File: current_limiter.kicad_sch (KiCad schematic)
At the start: 53 parts, among them J1 73096-2, J2 73096-2, J3 CS-, J4 CS+, J5 73096-2, J6 73096-2, Q1 BSC040N10NS5, Q2 BC849, Q3 BC858, U1 TLV1805QDBVRQ1, U2 INA181A2IDBVR, U3 OPA991IDCKR, U4 BAT54CLT3G, U5 LM4040DIM3-2.5/NOPB

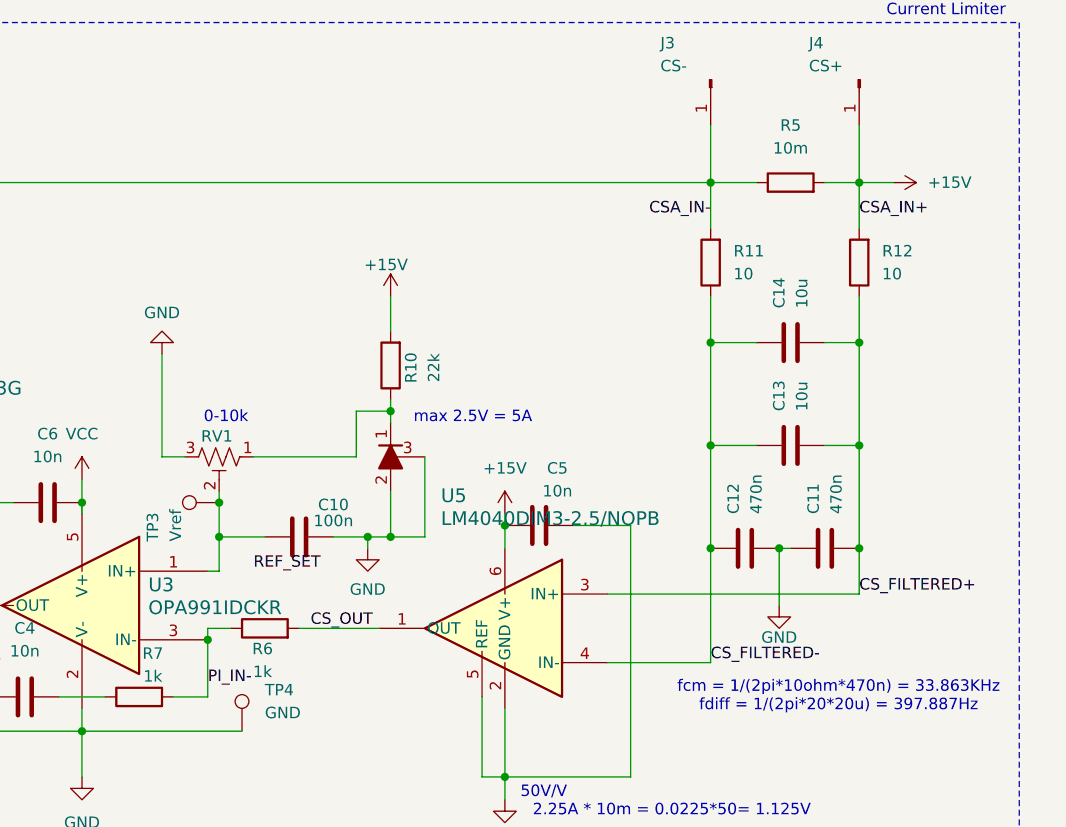
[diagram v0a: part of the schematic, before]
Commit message: minor updates: swapped out currentsense for in stock version, made sure all parts in stock, corrected Vs for currentsense
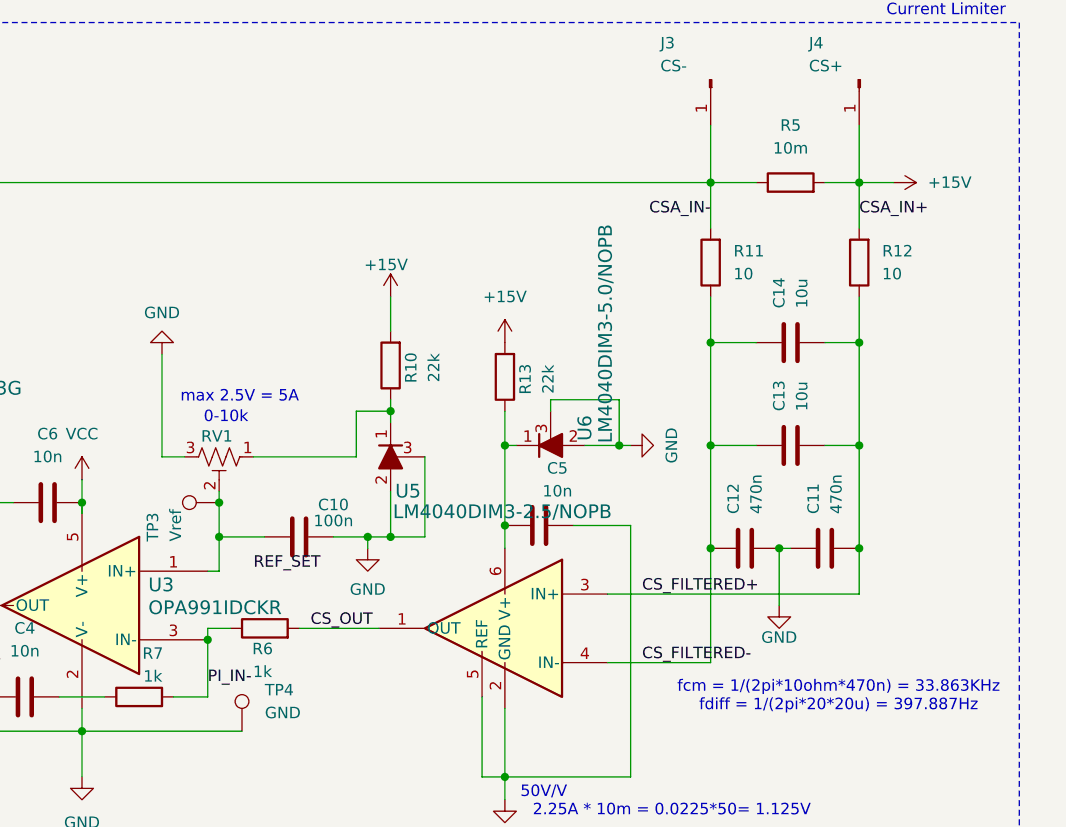
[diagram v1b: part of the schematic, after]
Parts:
- added R13: 22k, Capacitor_SMD:C_0805_2012Metric, symbol Device:R
- added U6: LM4040DIM3-5.0/NOPB, Current_Limiter_Stuff:DBZ3, symbol Current-limiter-stuff:LM4040DIM3-2.5_NOPB
- Q1: value BSC040N10NS5 -> ISC025N08NM5LF2
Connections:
- net +15V: now also R13.2; no longer C5.1, U2.6 (V+)
- net GND: now also U6.2, U6.3
- new net: C5.1, R13.1, U2.6 (V+), U6.1

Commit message: updated zeners to model thats actually in stock
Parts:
- removed D3, D5: BZV55B20, Diode_SMD:D_MiniMELF, symbol Diode:BZV55B20
- added CR1, CR2: BZT52C20-7-F, Current_Limiter_Stuff:SOD123_DIO, symbol Current-limiter-stuff:BZT52C20-7-F
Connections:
- net VBATT: now also CR1.1
- net fet_gate: now also CR2.1
- new net: CR1.2, CR2.2
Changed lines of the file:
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@@
 	)
 	(junction
+		(at 132.08 35.56)
+		(diameter 0)
+		(color 0 0 0 0)
+	)
+	(junction
 		(at 177.8 96.52)
 		(diameter 0)
@@
 	(wire
 		(pts
+			(xy 132.08 50.8) (xy 132.08 46.99)
+		)
+		(stroke
+			(width 0)
+			(type default)
+		)
+	)
+	(wire
+		(pts
 			(xy 186.69 66.04) (xy 189.23 66.04)
 		)
@@
 	(wire
 		(pts
+			(xy 121.92 40.64) (xy 121.92 46.99)
+		)
+		(stroke
+			(width 0)
+			(type default)
+		)
+	)
+	(wire
+		(pts
 			(xy 153.67 50.8) (xy 156.21 50.8)
 		)
@@
 	(wire
 		(pts
+			(xy 139.7 50.8) (xy 132.08 50.8)
+		)
+		(stroke
+			(width 0)
+			(type default)
+		)
+	)
+	(wire
+		(pts
 			(xy 99.06 46.99) (xy 99.06 54.61)
 		)
@@
 	(wire
 		(pts
-			(xy 128.27 50.8) (xy 139.7 50.8)
-		)
-		(stroke
-			(width 0)
-			(type default)
-		)
-	)
-	(wire
-		(pts
 			(xy 62.23 31.75) (xy 99.06 31.75)
 		)
@@
 	(wire
 		(pts
+			(xy 132.08 35.56) (xy 132.08 40.64)
+		)
+		(stroke
+			(width 0)
+			(type default)
+		)
+	)
+	(wire
+		(pts
 			(xy 193.04 69.85) (xy 193.04 71.12)
 		)
@@
 	)
 	(symbol
-		(lib_id "Diode:BZV55B20")
-		(at 128.27 39.37 270)
-		(unit 1)
-		(body_style 1)
-		(exclude_from_sim no)
-		(in_bom yes)
-		(on_board yes)
-		(in_pos_files yes)
-		(dnp no)
-		(fields_autoplaced yes)
-		(property "Reference" "D5"
-			(at 130.81 38.0999 90)
-			(show_name no)
-			(do_not_autoplace no)
-			(effects
-				(font
-					(size 1.27 1.27)
-				)
-				(justify left)
-			)
-		)
-		(property "Value" "BZV55B20"
-			(at 130.81 40.6399 90)
-			(show_name no)
-			(do_not_autoplace no)
-			(effects
-				(font
-					(size 1.27 1.27)
-				)
-				(justify left)
-			)
-		)
-		(property "Footprint" "Diode_SMD:D_MiniMELF"
-			(at 123.825 39.37 0)
-			(hide yes)
-			(show_name no)
-			(do_not_autoplace no)
-			(effects
-				(font
-					(size 1.27 1.27)
-				)
-			)
-		)
-		(property "Datasheet" "https://assets.nexperia.com/documents/data-sheet/BZV55_SER.pdf"
-			(at 128.27 39.37 0)
-			(hide yes)
-			(show_name no)
-			(do_not_autoplace no)
-			(effects
-				(font
-					(size 1.27 1.27)
-				)
-			)
-		)
-		(property "Description" "20V, 500mW, 2%, Zener diode, MiniMELF"
-			(at 128.27 39.37 0)
-			(hide yes)
-			(show_name no)
-			(do_not_autoplace no)
-			(effects
-				(font
-					(size 1.27 1.27)
-				)
-			)
-		)
-		(pin "1"
-		)
-		(pin "2"
-		)
-		(instances
-			(project "current_limiter"
-				(path "/9cad53dd-e6ec-4945-b0cd-3a61fa1e6914"
-					(reference "D5")
-					(unit 1)
-				)
-			)
-		)
-	)
-	(symbol
 		(lib_id "Device:R")
 		(at 139.7 62.23 180)
@@
 	)
 	(symbol
+		(lib_id "Current-limiter-stuff:BZT52C20-7-F")
+		(at 121.92 40.64 0)
+		(unit 1)
+		(body_style 1)
+		(exclude_from_sim no)
+		(in_bom yes)
+		(on_board yes)
+		(in_pos_files yes)
+		(dnp no)
+		(property "Reference" "CR1"
+			(at 116.84 36.576 0)
+			(show_name no)
+			(do_not_autoplace no)
+			(effects
+				(font
+					(size 1.524 1.524)
+				)
+			)
+		)
+		(property "Value" "BZT52C20-7-F"
+			(at 116.84 39.116 0)
+			(show_name no)
+			(do_not_autoplace no)
+			(effects
+				(font
+					(size 1.524 1.524)
+				)
+			)
+		)
+		(property "Footprint" "Current_Limiter_Stuff:SOD123_DIO"
+			(at 121.92 40.64 0)
+			(hide yes)
+			(show_name no)
+			(do_not_autoplace no)
+			(effects
+				(font
+					(size 1.27 1.27)
+					(italic yes)
+				)
+			)
+		)
+		(property "Datasheet" "BZT52C20-7-F"
+			(at 121.92 40.64 0)
+			(hide yes)
+			(show_name no)
+			(do_not_autoplace no)
+			(effects
+				(font
+					(size 1.27 1.27)
+					(italic yes)
+				)
+			)
+		)
+		(property "Description" ""
+			(at 121.92 40.64 0)
+			(hide yes)
+			(show_name no)
+			(do_not_autoplace no)
+			(effects
+				(font
+					(size 1.27 1.27)
+				)
+			)
+		)
+		(pin "1"
+		)
+		(pin "2"
+		)
+		(instances
+			(project "current_limiter"
+				(path "/9cad53dd-e6ec-4945-b0cd-3a61fa1e6914"
+					(reference "CR1")
+					(unit 1)
+				)
+			)
+		)
+	)
+	(symbol
 		(lib_id "Connector:TestPoint")
 		(at 195.58 96.52 0)
@@
 	)
 	(symbol
+		(lib_id "Current-limiter-stuff:BZT52C20-7-F")
+		(at 121.92 46.99 0)
+		(unit 1)
+		(body_style 1)
+		(exclude_from_sim no)
+		(in_bom yes)
+		(on_board yes)
+		(in_pos_files yes)
+		(dnp no)
+		(property "Reference" "CR2"
+			(at 137.922 52.07 0)
+			(show_name no)
+			(do_not_autoplace no)
+			(effects
+				(font
+					(size 1.524 1.524)
+				)
+			)
+		)
+		(property "Value" "BZT52C20-7-F"
+			(at 137.922 49.53 0)
+			(show_name no)
+			(do_not_autoplace no)
+			(effects
+				(font
+					(size 1.524 1.524)
+				)
+			)
+		)
+		(property "Footprint" "Current_Limiter_Stuff:SOD123_DIO"
+			(at 121.92 46.99 0)
+			(hide yes)
+			(show_name no)
+			(do_not_autoplace no)
+			(effects
+				(font
+					(size 1.27 1.27)
+					(italic yes)
+				)
+			)
+		)
+		(property "Datasheet" "BZT52C20-7-F"
+			(at 121.92 46.99 0)
+			(hide yes)
+			(show_name no)
+			(do_not_autoplace no)
+			(effects
+				(font
+					(size 1.27 1.27)
+					(italic yes)
+				)
+			)
+		)
+		(property "Description" ""
+			(at 121.92 46.99 0)
+			(hide yes)
+			(show_name no)
+			(do_not_autoplace no)
+			(effects
+				(font
+					(size 1.27 1.27)
+				)
+			)
+		)
+		(pin "1"
+		)
+		(pin "2"
+		)
+		(instances
+			(project "current_limiter"
+				(path "/9cad53dd-e6ec-4945-b0cd-3a61fa1e6914"
+					(reference "CR2")
+					(unit 1)
+				)
+			)
+		)
+	)
+	(symbol
 		(lib_id "Device:R")
 		(at 247.65 44.45 180)
@@
 					(unit 1)
 				)
-			)
-		)
-	)
-	(symbol
-		(lib_id "Diode:BZV55B20")
-		(at 128.27 46.99 90)
-		(unit 1)
-		(body_style 1)
-		(exclude_from_sim no)
-		(in_bom yes)
-		(on_board yes)
-		(in_pos_files yes)
-		(dnp no)
-		(fields_autoplaced yes)
-		(property "Reference" "D3"
-			(at 130.81 45.7199 90)
-			(show_name no)
-			(do_not_autoplace no)
-			(effects
-				(font
-					(size 1.27 1.27)
-				)
-				(justify right)
-			)
-		)
-		(property "Value" "BZV55B20"
-			(at 130.81 48.2599 90)
-			(show_name no)
-			(do_not_autoplace no)
-			(effects
-				(font
-					(size 1.27 1.27)
-				)
-				(justify right)
-			)
-		)
-		(property "Footprint" "Diode_SMD:D_MiniMELF"
-			(at 132.715 46.99 0)
-			(hide yes)
-			(show_name no)
-			(do_not_autoplace no)
-			(effects
-				(font
-					(size 1.27 1.27)
-				)
-			)
-		)
-		(property "Datasheet" "https://assets.nexperia.com/documents/data-sheet/BZV55_SER.pdf"
-			(at 128.27 46.99 0)
-			(hide yes)
-			(show_name no)
-			(do_not_autoplace no)
-			(effects
-				(font
-					(size 1.27 1.27)
-				)
-			)
-		)
-		(property "Description" "20V, 500mW, 2%, Zener diode, MiniMELF"
-			(at 128.27 46.99 0)
-			(hide yes)
-			(show_name no)
-			(do_not_autoplace no)
-			(effects
-				(font
-					(size 1.27 1.27)
-				)
-			)
-		)
-		(pin "1"
-		)
-		(pin "2"
-		)
-		(instances
-			(project "current_limiter"
-				(path "/9cad53dd-e6ec-4945-b0cd-3a61fa1e6914"
-					(reference "D3")
-					(unit 1)
-				)

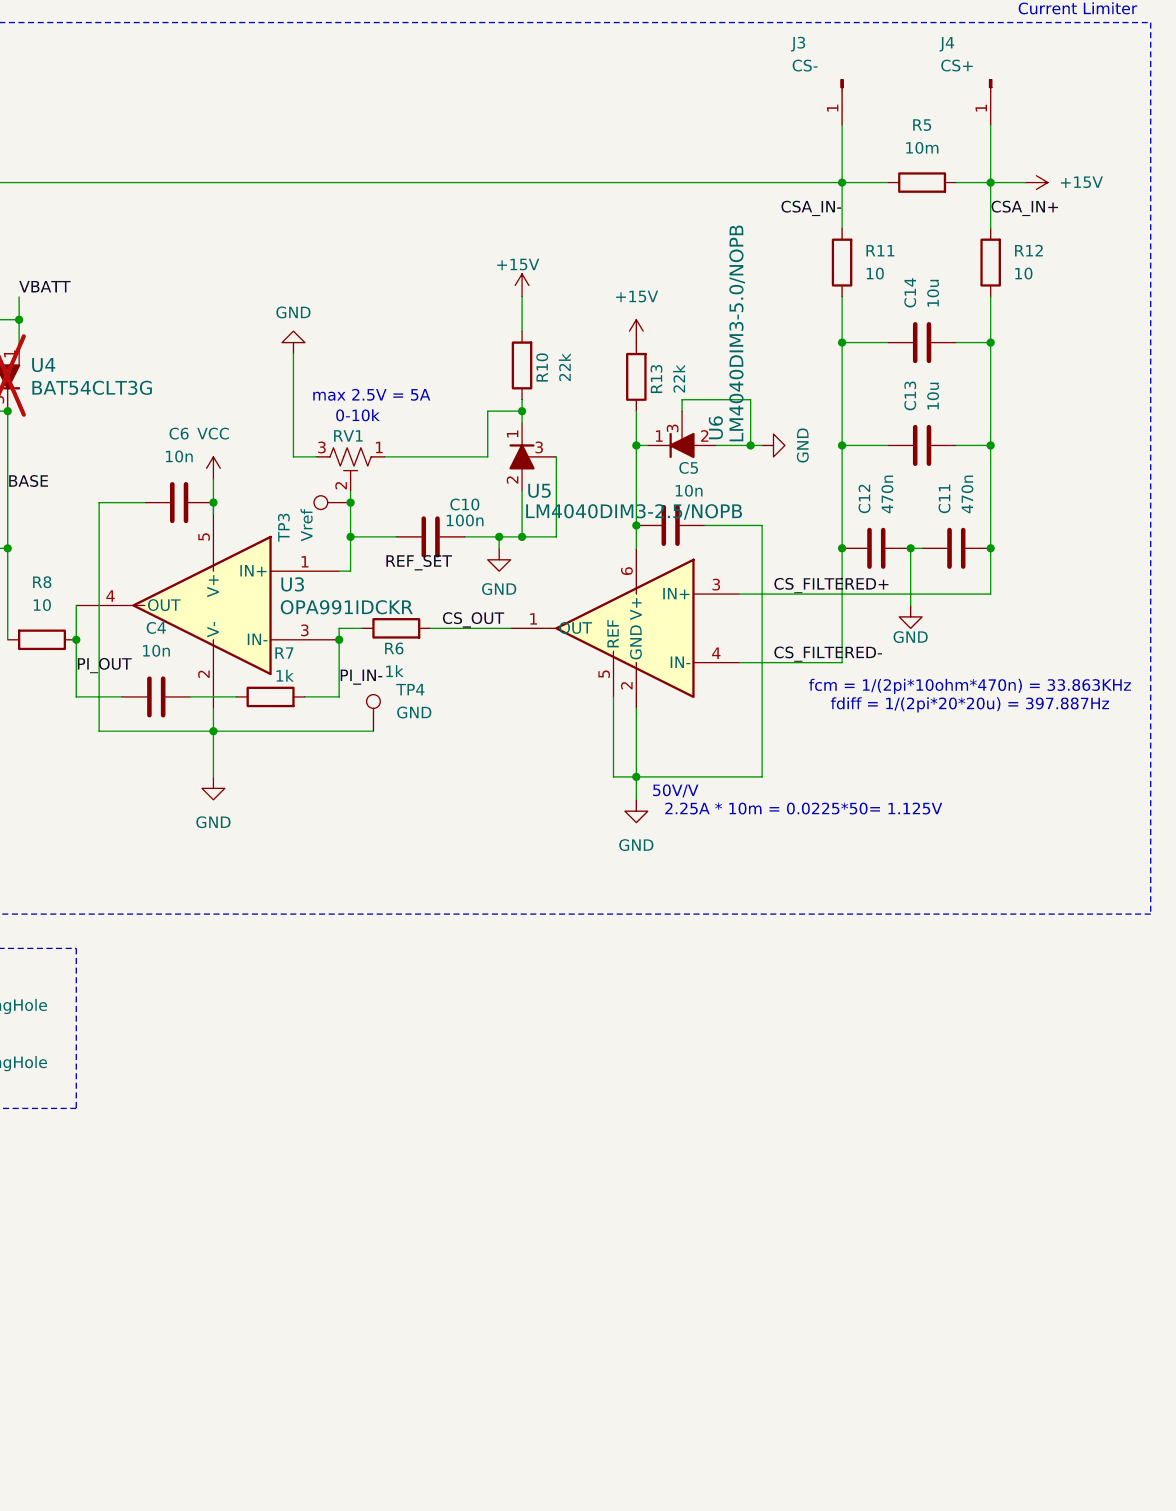
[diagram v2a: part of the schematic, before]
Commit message: updated all passive components to 805 footprint, added 3V3 regulator for currentsense
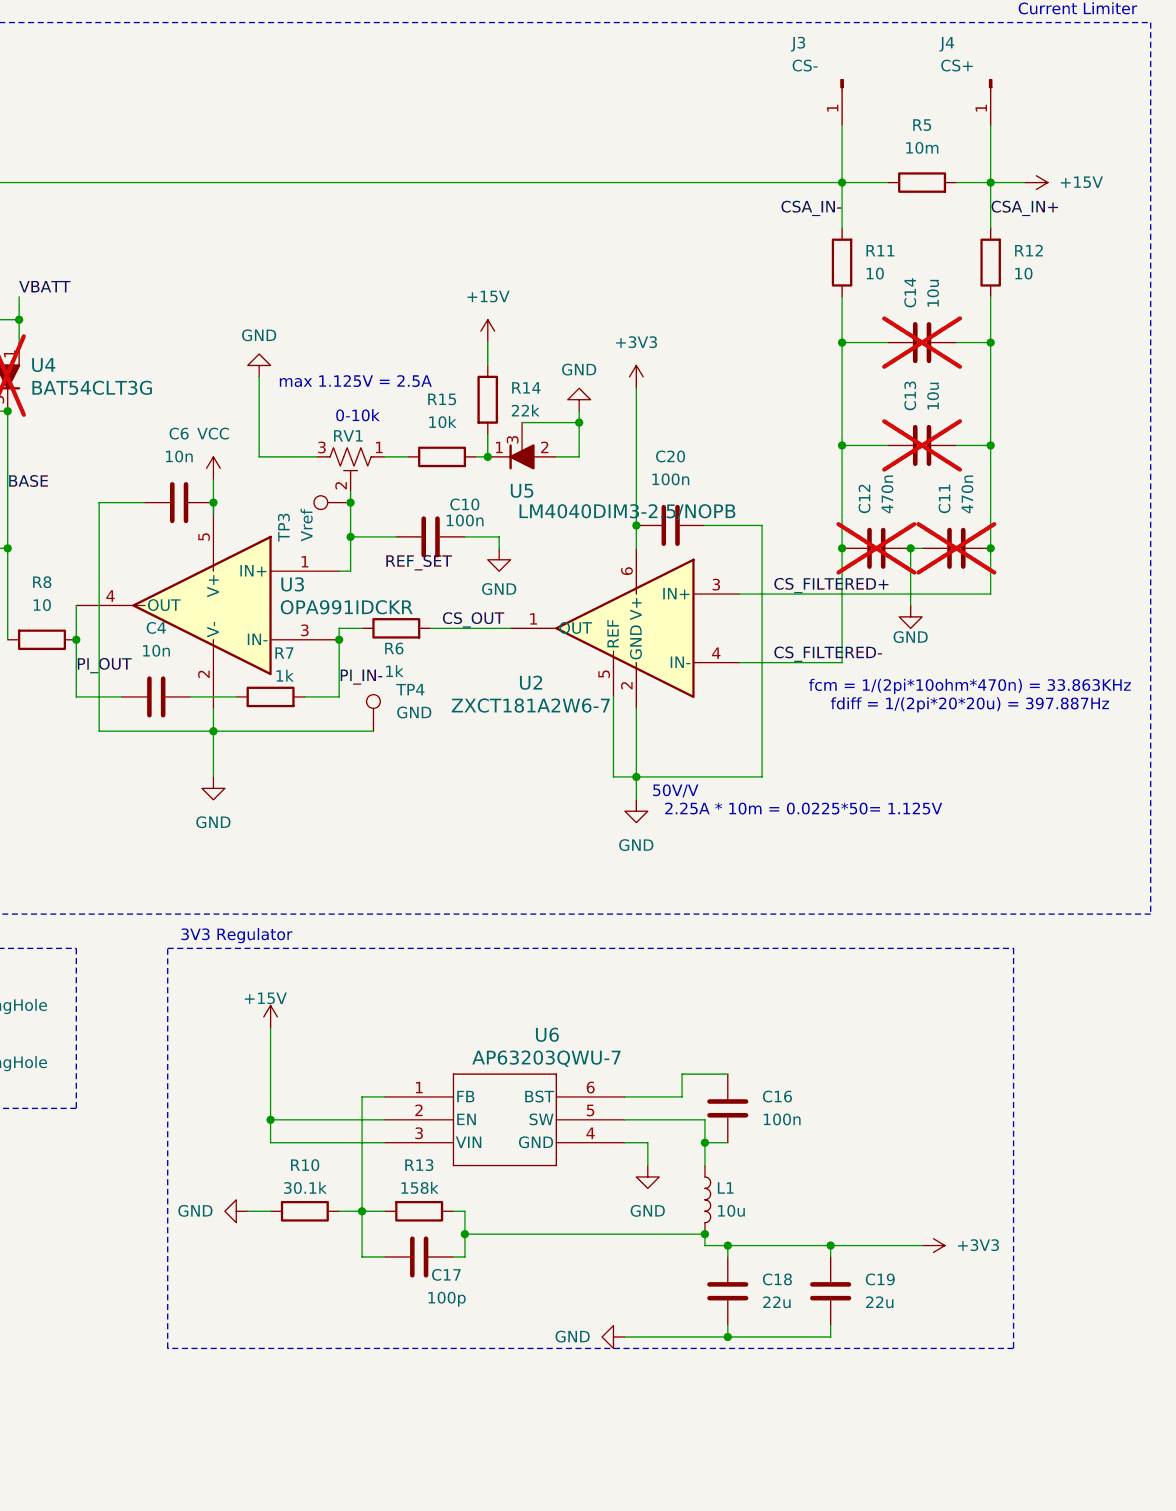
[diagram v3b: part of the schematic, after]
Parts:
- removed C5: 10n, Capacitor_SMD:C_0402_1005Metric, symbol Device:C
- removed U6: LM4040DIM3-5.0/NOPB, Current_Limiter_Stuff:DBZ3, symbol Current-limiter-stuff:LM4040DIM3-2.5_NOPB
- added C16, C20: 100n, Capacitor_SMD:C_0805_2012Metric, symbol Device:C
- added C17: 100p, Capacitor_SMD:C_0805_2012Metric, symbol Device:C
- added C18, C19: 22u, Capacitor_SMD:C_0805_2012Metric, symbol Device:C
- added L1: 10u, Inductor_SMD:L_0805_2012Metric, symbol Device:L
- added R14: 22k, Resistor_SMD:R_0805_2012Metric, symbol Device:R
- added R15: 10k, Resistor_SMD:R_0805_2012Metric, symbol Device:R
- added U6: AP63203QWU-7, Current_Limiter_Stuff:TSOT26_DIO, symbol Current-limiter-stuff:AP63203QWU-7
- C1, C6, C7: footprint Capacitor_SMD:C_0402_1005Metric -> Capacitor_SMD:C_0805_2012Metric
- C11, C12, C13, C14: footprint Capacitor_SMD:C_0402_1005Metric -> Capacitor_SMD:C_0805_2012Metric; now not fitted
- R1, R11, R12, R2, R3, R4, R8: footprint Resistor_SMD:R_0402_1005Metric -> Resistor_SMD:R_0805_2012Metric
- R10: value 22k -> 30.1k; footprint Capacitor_SMD:C_0805_2012Metric -> Resistor_SMD:R_0805_2012Metric
- R13: value 22k -> 158k; footprint Capacitor_SMD:C_0805_2012Metric -> Resistor_SMD:R_0805_2012Metric
- R6, R7: footprint Capacitor_SMD:C_0805_2012Metric -> Resistor_SMD:R_0805_2012Metric
- U2: value INA181A2IDBVR -> ZXCT181A2W6-7
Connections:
- net +15V: now also R14.1, U6.2 (EN), U6.3 (VIN); no longer R10.2, R13.2
- net GND: now also R10.2, C18.2, C19.2, C20.2, U6.4 (GND)
- net +3V3: now reaches R13.1, U2.6 (V+)
- net +3V3: now also C17.2, C18.1, C19.1, C20.1, L1.2
- new net: C16.2, L1.1, U6.5 (SW)
- new net: R15.1, RV1.1
- new net: R14.2, R15.2, U5.1
- new net: C17.1, R10.1, R13.2, U6.1 (FB)
- new net: C16.1, U6.6 (BST)
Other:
- note added: "3V3 Regulator"
- note added: "max 1.125V = 2.5A"
- note removed: "max 2.5V = 5A"
